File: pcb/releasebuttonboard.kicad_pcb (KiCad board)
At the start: 2 copper layers, 65 x 56 mm, 30 parts, among them SW1 ROTENC, U1 24C16, U2 RASPIPLUSHEADER, U3 OLEDHeader, U4 REncHeader, U5 BtnHeader, U6 PAM8407, U7 REncHeader

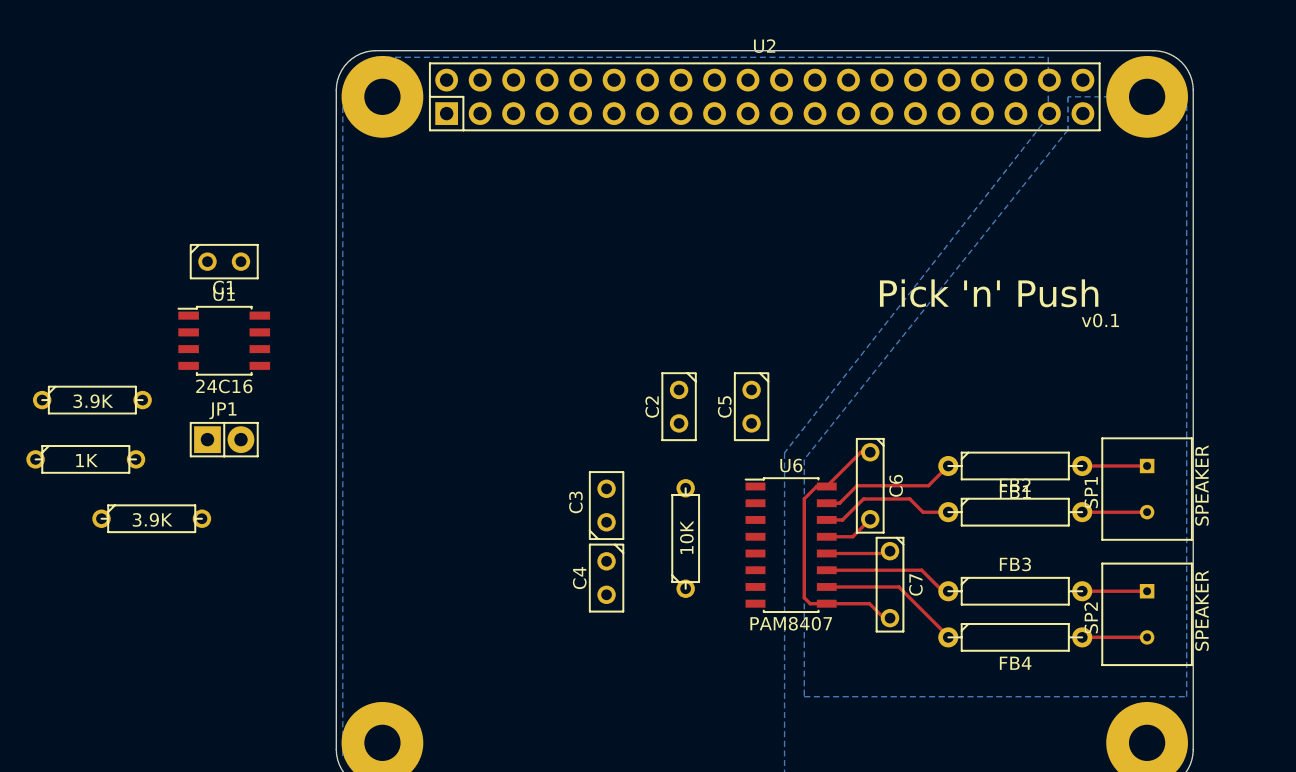
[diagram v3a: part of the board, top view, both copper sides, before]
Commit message: Starting to lay out the EEPROM curcuit and unamped audio.
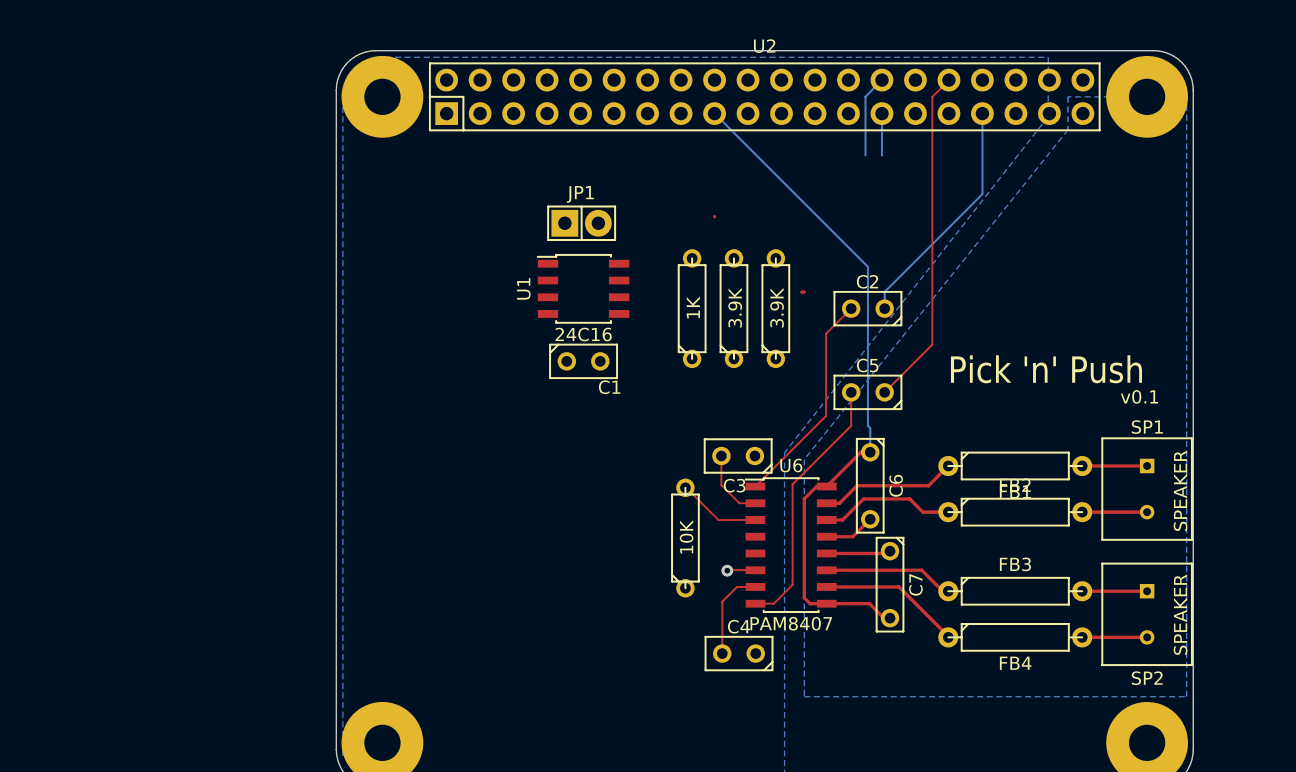
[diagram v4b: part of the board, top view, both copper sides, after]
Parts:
- moved R2 52.3 mm to (128.8, 87.6), turned to 90 degrees
- moved R1 47.4 mm to (122.5, 87.6), turned to 90 degrees
- moved R3 47.0 mm to (125.7, 87.6), turned to 90 degrees
- moved JP1 31.7 mm to (114.1, 81.1)
- moved C1 28.3 mm to (114.3, 91.6)
- moved U1 27.5 mm to (114.3, 86.1)
- moved C2 16.1 mm to (135.8, 87.6), turned to 180 degrees
- moved C4 11.6 mm to (126.0, 113.7), turned to 180 degrees
- moved C3 10.7 mm to (126.0, 98.7), turned to 180 degrees
- moved C5 8.89 mm to (135.8, 93.9), turned to 180 degrees
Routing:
- net VCC: track 21.1 -> 52.2 mm
- net /AUD_L: track 0.00 -> 25.7 mm
- net Net-(C5-Pad2): track 0.00 -> 19.8 mm
- net /AUD_R: track 0.00 -> 17.9 mm
- net Net-(C2-Pad2): track 0.00 -> 16.5 mm
- net Net-(C4-Pad2): track 0.00 -> 6.92 mm
- net Net-(R4-Pad2): track 0.00 -> 6.33 mm
- net /ID_SC: track 0.00 -> 6.23 mm
- net Net-(C3-Pad2): track 0.00 -> 5.37 mm
- net /ID_SD: track 0.00 -> 3.18 mm
- net GND: track 8.72 -> 10.9 mm, vias 0 -> 1
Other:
- net class Default: clearance 0.254 -> 0.1524; trace_width 0.254 -> 0.1524
- rule trace_clearance: 0.254 -> 0.1524
- rule trace_min: 0.254 -> 0.1524

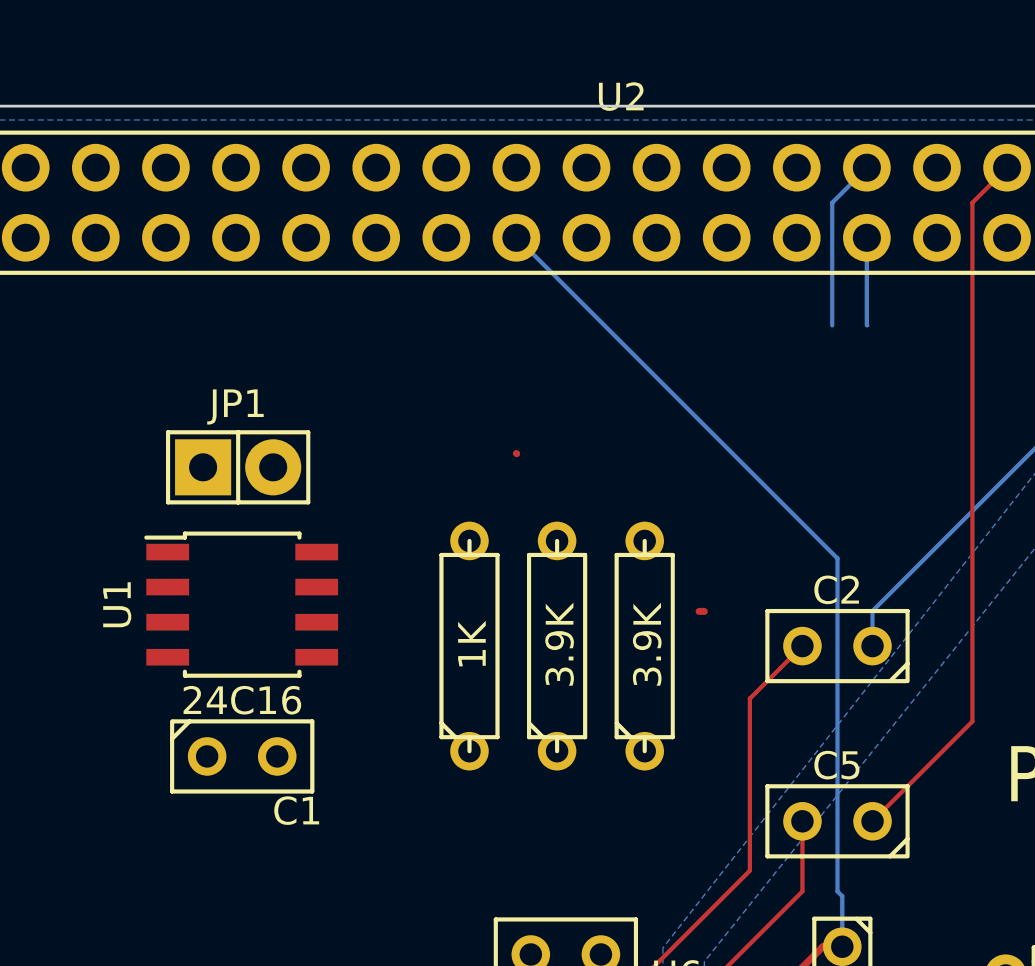
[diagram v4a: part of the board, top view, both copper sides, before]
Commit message: Further PCB traces and tweaks.
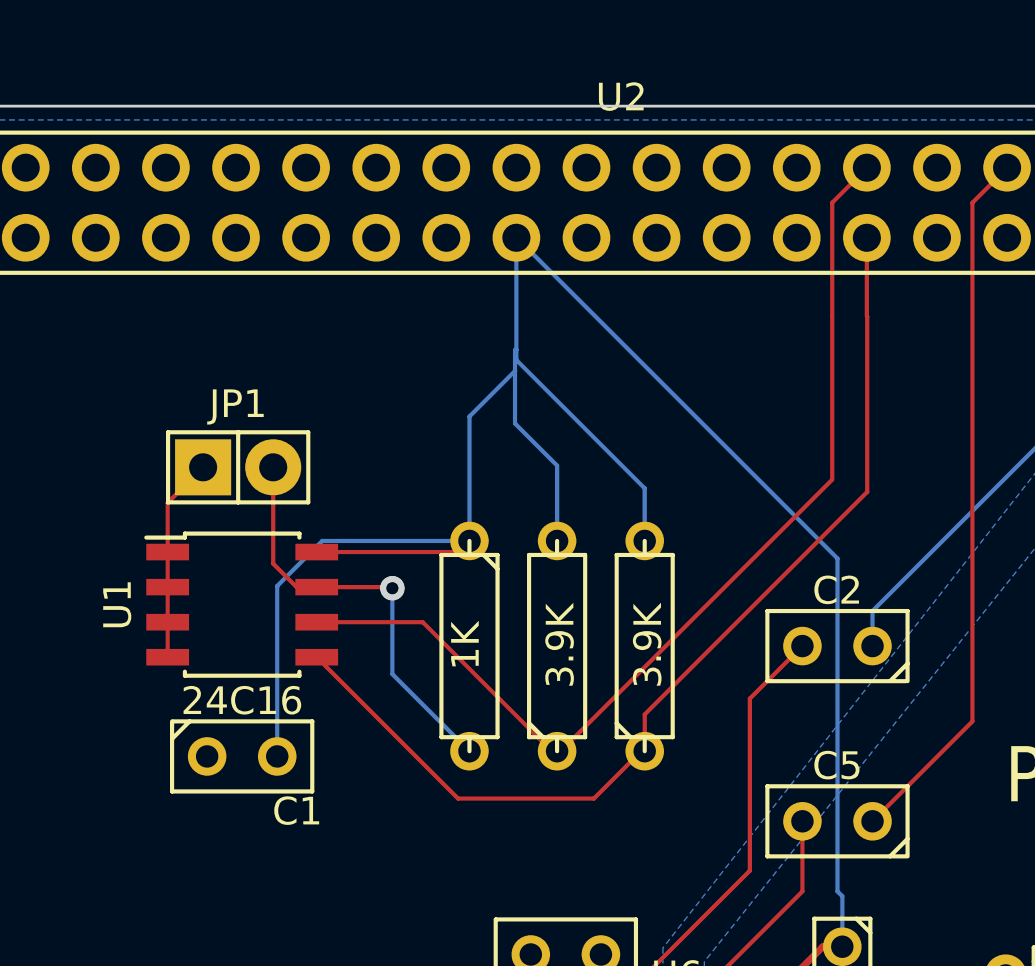
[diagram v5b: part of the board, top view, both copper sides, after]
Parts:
- turned R1 to 270 degrees
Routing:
- net VCC: track 52.2 -> 99.1 mm
- net /ID_SD: track 3.18 -> 36.7 mm
- net /ID_SC: track 6.23 -> 36.5 mm
- net Net-(JP1-Pad2): track 0.00 -> 15.2 mm, vias 0 -> 1
- net GND: track 10.9 -> 18.3 mm
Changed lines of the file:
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@@
   (general
     (links 75)
-    (no_connects 43)
+    (no_connects 28)
     (area 95.449999 67.949999 160.550001 124.050001)
     (thickness 1.6)
     (drawings 10)
-    (tracks 75)
+    (tracks 115)
     (zones 0)
     (modules 30)
@@
   )
   (module Discret:R3 (layer F.Cu)
-    (at 122.49 87.565 90)
+    (at 122.49 87.565 270)
     (descr "Resitance 3 pas")
     (tags R)
     (autoplace_cost180 10)
-    (fp_text reference R1 (at 0 -2 90) (layer F.SilkS) hide
-      (effects (font (size 1 1) (thickness 0.15)))
-    )
-    (fp_text value 1K (at 0 0.127 90) (layer F.SilkS)
+    (fp_text reference R1 (at 0 -2 270) (layer F.SilkS) hide
+      (effects (font (size 1 1) (thickness 0.15)))
+    )
+    (fp_text value 1K (at 0 0.127 450) (layer F.SilkS)
       (effects (font (size 1 1) (thickness 0.15)))
     )
@@
     (fp_line (start 3.302 1.016) (end 3.302 0) (layer F.SilkS) (width 0.15))
     (fp_line (start -3.302 -0.508) (end -2.794 -1.016) (layer F.SilkS) (width 0.15))
-    (pad 1 thru_hole circle (at -3.81 0 90) (size 1.397 1.397) (drill 0.8128) (layers *.Cu *.Mask F.SilkS)
-      (net 2 VCC))
-    (pad 2 thru_hole circle (at 3.81 0 90) (size 1.397 1.397) (drill 0.8128) (layers *.Cu *.Mask F.SilkS)
+    (pad 1 thru_hole circle (at -3.81 0 270) (size 1.397 1.397) (drill 0.8128) (layers *.Cu *.Mask F.SilkS)
+      (net 2 VCC))
+    (pad 2 thru_hole circle (at 3.81 0 270) (size 1.397 1.397) (drill 0.8128) (layers *.Cu *.Mask F.SilkS)
       (net 17 "Net-(JP1-Pad2)"))
     (model Discret/R3.wrl
@@
   (gr_line (start 95.5 71) (end 95.5 121) (angle 90) (layer Edge.Cuts) (width 0.1))
   (gr_arc (start 98.5 71) (end 95.5 71) (angle 90) (layer Edge.Cuts) (width 0.1))
-  (segment (start 124.19 80.585) (end 124.2 80.595) (width 0.254) (layer F.Cu) (net 0))
-  (segment (start 131 86.31) (end 130.81 86.31) (width 0.254) (layer F.Cu) (net 0))
+  (segment (start 111.554 87.969) (end 111.554 86.699) (width 0.1524) (layer F.Cu) (net 1) (status C00000))
+  (segment (start 111.554 86.699) (end 111.554 85.429) (width 0.1524) (layer F.Cu) (net 1) (status C00000))
+  (segment (start 111.554 85.429) (end 111.554 84.159) (width 0.1524) (layer F.Cu) (net 1) (status C00000))
+  (segment (start 111.554 84.159) (end 111.554 82.372) (width 0.1524) (layer F.Cu) (net 1) (status 400000))
+  (segment (start 111.554 82.372) (end 112.838 81.088) (width 0.1524) (layer F.Cu) (net 1) (status 800000))
   (segment (start 127.3 107.405) (end 125.1925 107.405) (width 0.1524) (layer F.Cu) (net 1))
   (via (at 125.157 107.4405) (size 0.889) (layers F.Cu B.Cu) (net 1))
@@
   (segment (start 132.7 104.865) (end 134.675 104.865) (width 0.254) (layer F.Cu) (net 1))
   (segment (start 134.675 104.865) (end 136 103.54) (width 0.254) (layer F.Cu) (net 1))
+  (segment (start 115.524 91.564) (end 115.524 85.387) (width 0.1524) (layer B.Cu) (net 2) (status 400000))
+  (segment (start 117.156 83.755) (end 122.49 83.755) (width 0.1524) (layer B.Cu) (net 2) (status 800000))
+  (segment (start 115.524 85.387) (end 117.156 83.755) (width 0.1524) (layer B.Cu) (net 2))
+  (segment (start 116.954 84.159) (end 122.086 84.159) (width 0.1524) (layer F.Cu) (net 2) (status C00000))
+  (segment (start 122.086 84.159) (end 122.49 83.755) (width 0.1524) (layer F.Cu) (net 2) (status C00000))
+  (segment (start 122.49 83.755) (end 122.49 79.2465) (width 0.1524) (layer B.Cu) (net 2))
+  (segment (start 122.49 79.2465) (end 124.141 77.5955) (width 0.1524) (layer B.Cu) (net 2))
+  (segment (start 125.665 83.755) (end 125.665 81.0245) (width 0.1524) (layer B.Cu) (net 2))
+  (segment (start 124.141 76.8335) (end 124.19 76.8335) (width 0.1524) (layer B.Cu) (net 2))
+  (segment (start 124.141 79.5005) (end 124.141 77.5955) (width 0.1524) (layer B.Cu) (net 2))
+  (segment (start 124.141 77.5955) (end 124.141 76.8335) (width 0.1524) (layer B.Cu) (net 2))
+  (segment (start 125.665 81.0245) (end 124.141 79.5005) (width 0.1524) (layer B.Cu) (net 2))
+  (segment (start 128.84 83.755) (end 128.84 81.85) (width 0.1524) (layer B.Cu) (net 2))
+  (segment (start 124.19 77.2) (end 124.19 76.8335) (width 0.1524) (layer B.Cu) (net 2))
+  (segment (start 124.19 76.8335) (end 124.19 72.77) (width 0.1524) (layer B.Cu) (net 2))
+  (segment (start 128.84 81.85) (end 124.19 77.2) (width 0.1524) (layer B.Cu) (net 2))
   (segment (start 135.825 84.39) (end 135.825 96.455) (width 0.1524) (layer B.Cu) (net 2))
   (segment (start 124.205 72.77) (end 135.825 84.39) (width 0.1524) (layer B.Cu) (net 2))
@@
   (segment (start 138.175 108.675) (end 132.7 108.675) (width 0.254) (layer F.Cu) (net 15))
   (segment (start 157 112.5) (end 152.08 112.5) (width 0.254) (layer F.Cu) (net 16))
-  (segment (start 136.89 72.77) (end 136.89 75.93) (width 0.1524) (layer B.Cu) (net 18))
-  (segment (start 136.89 75.93) (end 136.9045 75.9445) (width 0.1524) (layer B.Cu) (net 18))
-  (segment (start 136.89 70.23) (end 136.89 70.244) (width 0.1524) (layer B.Cu) (net 19))
-  (segment (start 136.89 70.244) (end 135.6345 71.4995) (width 0.1524) (layer B.Cu) (net 19))
-  (segment (start 135.6345 71.4995) (end 135.6345 75.9445) (width 0.1524) (layer B.Cu) (net 19))
-  (segment (start 121.982 101.154) (end 122.0455 101.154) (width 0.1524) (layer F.Cu) (net 20) (status C00000))
-  (segment (start 122.0455 101.154) (end 124.4865 103.595) (width 0.1524) (layer F.Cu) (net 20) (status 400000))
-  (segment (start 124.4865 103.595) (end 127.3 103.595) (width 0.1524) (layer F.Cu) (net 20) (status 800000))
+  (segment (start 116.954 85.429) (end 116.2265 85.429) (width 0.1524) (layer F.Cu) (net 17) (status C00000))
+  (segment (start 116.2265 85.429) (end 115.378 84.5805) (width 0.1524) (layer F.Cu) (net 17) (status 400000))
+  (segment (start 115.378 84.5805) (end 115.378 81.088) (width 0.1524) (layer F.Cu) (net 17) (status 800000))
+  (segment (start 122.49 91.375) (end 119.696 88.581) (width 0.1524) (layer B.Cu) (net 17))
+  (segment (start 119.6555 85.429) (end 116.954 85.429) (width 0.1524) (layer F.Cu) (net 17))
+  (segment (start 119.696 85.4695) (end 119.6555 85.429) (width 0.1524) (layer F.Cu) (net 17))
+  (via (at 119.696 85.4695) (size 0.889) (layers F.Cu B.Cu) (net 17))
+  (segment (start 119.696 88.581) (end 119.696 85.4695) (width 0.1524) (layer B.Cu) (net 17))
+  (segment (start 128.84 91.375) (end 128.713 91.375) (width 0.1524) (layer F.Cu) (net 18))
+  (segment (start 128.713 91.375) (end 126.9985 93.0895) (width 0.1524) (layer F.Cu) (net 18))
+  (segment (start 122.0745 93.0895) (end 116.954 87.969) (width 0.1524) (layer F.Cu) (net 18))
+  (segment (start 126.9985 93.0895) (end 122.0745 93.0895) (width 0.1524) (layer F.Cu) (net 18))
+  (segment (start 128.84 91.375) (end 128.84 90.0415) (width 0.1524) (layer F.Cu) (net 18))
+  (segment (start 136.89 75.6125) (end 136.9045 75.627) (width 0.1524) (layer F.Cu) (net 18))
+  (segment (start 136.89 75.6125) (end 136.89 72.77) (width 0.1524) (layer F.Cu) (net 18))
+  (segment (start 136.9045 81.977) (end 136.9045 75.627) (width 0.1524) (layer F.Cu) (net 18))
+  (segment (start 128.84 90.0415) (end 136.9045 81.977) (width 0.1524) (layer F.Cu) (net 18))
+  (segment (start 125.665 91.375) (end 125.4745 91.375) (width 0.1524) (layer F.Cu) (net 19))
+  (segment (start 125.4745 91.375) (end 120.7985 86.699) (width 0.1524) (layer F.Cu) (net 19))
+  (segment (start 120.7985 86.699) (end 116.954 86.699) (width 0.1524) (layer F.Cu) (net 19))
+  (segment (start 125.665 91.375) (end 125.792 91.375) (width 0.1524) (layer F.Cu) (net 19))
+  (segment (start 125.792 91.375) (end 135.6345 81.5325) (width 0.1524) (layer F.Cu) (net 19))
+  (segment (start 135.6345 81.5325) (end 135.6345 75.627) (width 0.1524) (layer F.Cu) (net 19))
+  (segment (start 136.89 70.23) (end 136.89 70.244) (width 0.1524) (layer F.Cu) (net 19))
+  (segment (start 136.89 70.244) (end 135.6345 71.4995) (width 0.1524) (layer F.Cu) (net 19))
+  (segment (start 135.6345 71.4995) (end 135.6345 75.627) (width 0.1524) (layer F.Cu) (net 19))
+  (segment (start 121.982 101.154) (end 122.0455 101.154) (width 0.1524) (layer F.Cu) (net 20))
+  (segment (start 122.0455 101.154) (end 124.4865 103.595) (width 0.1524) (layer F.Cu) (net 20))
+  (segment (start 124.4865 103.595) (end 127.3 103.595) (width 0.1524) (layer F.Cu) (net 20))
   (zone (net 1) (net_name GND) (layer B.Cu) (hatch edge 0.508)
     (connect_pads (clearance 0.508))
